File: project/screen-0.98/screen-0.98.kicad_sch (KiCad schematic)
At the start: 34 parts, among them J1 TFT_0.96_13, J2 Conn_01x06_Female, J3 USB_C_6pin, J4 Conn_01x02_Female, SW1 SW_DPDT_x2, SW2 SW_Push, SW3 SW_Push, U1 SPX3819M5-L-3-3, U2 ESP-12E, U3 TP4056_[C16581]

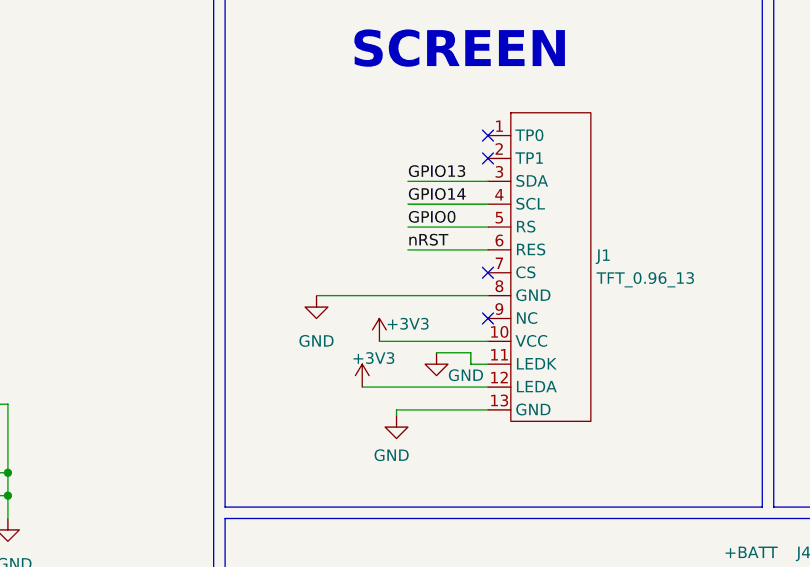
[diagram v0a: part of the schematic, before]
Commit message: fix: screen rst and cs
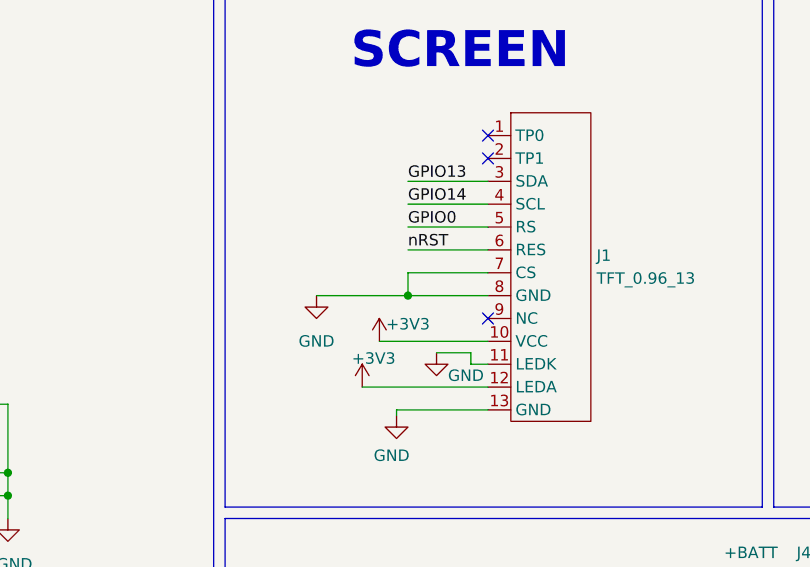
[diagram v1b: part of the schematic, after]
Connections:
- net GND: now also J1.7 (CS)
- no-connect marks 13 -> 12
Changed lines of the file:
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@@
   (junction (at 152.4 139.7) (diameter 0) (color 0 0 0 0)
+  )
+  (junction (at 196.85 117.475) (diameter 0) (color 0 0 0 0)
   )
   (junction (at 31.75 149.86) (diameter 0) (color 0 0 0 0)
@@
   (no_connect (at 85.09 49.53))
   (no_connect (at 50.8 129.54))
-  (no_connect (at 205.74 114.935))
   (no_connect (at 238.76 48.26))
   (no_connect (at 85.09 52.07))
@@
     (stroke (width 0) (type default) (color 0 0 0 0))
   )
+  (wire (pts (xy 205.74 114.935) (xy 196.85 114.935))
+    (stroke (width 0) (type default) (color 0 0 0 0))
+  )
   (polyline (pts (xy 176.53 80.01) (xy 236.22 80.01))
     (stroke (width 0) (type default) (color 0 0 0 0))
@@
     (stroke (width 0) (type default) (color 0 0 0 0))
   )
+  (wire (pts (xy 196.85 117.475) (xy 205.74 117.475))
+    (stroke (width 0) (type default) (color 0 0 0 0))
+  )
   (polyline (pts (xy 12.7 12.7) (xy 12.7 78.74))
     (stroke (width 0) (type default) (color 0 0 0 0))
@@
     (stroke (width 0) (type default) (color 0 0 0 0))
   )
+  (wire (pts (xy 196.85 114.935) (xy 196.85 117.475))
+    (stroke (width 0) (type default) (color 0 0 0 0))
+  )
   (wire (pts (xy 64.77 62.23) (xy 64.77 64.77))
     (stroke (width 0) (type default) (color 0 0 0 0))
@@
     (stroke (width 0) (type default) (color 0 0 0 0))
   )
-  (wire (pts (xy 186.69 117.475) (xy 205.74 117.475))
-    (stroke (width 0) (type default) (color 0 0 0 0))
-  )
+  (wire (pts (xy 186.69 117.475) (xy 196.85 117.475))
+    (stroke (width 0) (type default) (color 0 0 0 0))
+  )

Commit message: update 0.98
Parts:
- added Q1: S8050, Package_TO_SOT_SMD:SOT-23, symbol Device:Q_NPN_BEC
- added R15: 1K, Resistor_SMD:R_0402_1005Metric, symbol Device:R
- added R16: 12K, Resistor_SMD:R_0402_1005Metric, symbol Device:R
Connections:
- net +3V3: now also R16.1
- net GND: now also Q1.2 (E); no longer J1.11 (LEDK)
- net GPIO2: now also J1.6 (RES)
- net GPIO5: now also R15.1
- net nRST: no longer J1.6 (RES)
- new net: Q1.1 (B), R15.2, R16.2
- new net: J1.11 (LEDK), Q1.3 (C)
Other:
- moved on the sheet: J1

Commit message: feat: screen v1.3 done
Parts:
- removed J2: Conn_01x06_Female, Connector_PinHeader_1.27mm:PinHeader_1x06_P1.27mm_Vertical, symbol Connector:Conn_01x06_Female
- added J?: TTL-connect-pin4, symbol My-lib:TTL-connect-pin4
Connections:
- net GND: now also J?.1 (GND)
- net GPIO0: now also J?.2 (GPIO0)
- net RXD: now also J?.3 (RXD)
- net TXD: now also J?.4 (TXD)
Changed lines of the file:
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@@
-    (stroke (width 0) (type default) (color 0 0 0 0))
-  )
-  (wire (pts (xy 256.54 124.46) (xy 265.43 124.46))
     (stroke (width 0) (type default) (color 0 0 0 0))
   )
@@
     (stroke (width 0) (type default) (color 0 0 0 0))
   )
-  (wire (pts (xy 256.54 119.38) (xy 265.43 119.38))
-    (stroke (width 0) (type default) (color 0 0 0 0))
-  )
   (wire (pts (xy 31.75 149.86) (xy 31.75 151.13))
     (stroke (width 0) (type default) (color 0 0 0 0))
@@
     (stroke (width 0) (type default) (color 0 0 0 0))
   )
+  (wire (pts (xy 251.46 117.475) (xy 258.445 117.475))
+    (stroke (width 0) (type default) (color 0 0 0 0))
+  )
   (wire (pts (xy 175.26 57.15) (xy 182.88 57.15))
     (stroke (width 0) (type default) (color 0 0 0 0))
@@
     (stroke (width 0) (type default) (color 0 0 0 0))
   )
+  (wire (pts (xy 249.555 109.855) (xy 258.445 109.855))
+    (stroke (width 0) (type default) (color 0 0 0 0))
+  )
   (wire (pts (xy 200.914 119.38) (xy 211.074 119.38))
     (stroke (width 0) (type default) (color 0 0 0 0))
@@
     (stroke (width 0) (type default) (color 0 0 0 0))
   )
-  (wire (pts (xy 252.73 116.84) (xy 265.43 116.84))
+  (wire (pts (xy 249.555 114.935) (xy 258.445 114.935))
     (stroke (width 0) (type default) (color 0 0 0 0))
   )
@@
     (stroke (width 0) (type default) (color 0 0 0 0))
   )
-  (wire (pts (xy 256.54 127) (xy 265.43 127))
-    (stroke (width 0) (type default) (color 0 0 0 0))
-  )
   (wire (pts (xy 115.57 41.91) (xy 124.46 41.91))
     (stroke (width 0) (type default) (color 0 0 0 0))
@@
     (stroke (width 0) (type default) (color 0 0 0 0))
   )
-  (wire (pts (xy 256.54 121.92) (xy 265.43 121.92))
-    (stroke (width 0) (type default) (color 0 0 0 0))
-  )
   (wire (pts (xy 100.33 147.32) (xy 100.33 142.24))
     (stroke (width 0) (type default) (color 0 0 0 0))
@@
     (stroke (width 0) (type default) (color 0 0 0 0))
   )
-  (wire (pts (xy 256.54 114.3) (xy 265.43 114.3))
-    (stroke (width 0) (type default) (color 0 0 0 0))
-  )
   (wire (pts (xy 96.52 137.16) (xy 100.33 137.16))
     (stroke (width 0) (type default) (color 0 0 0 0))
@@
   )
   (polyline (pts (xy 237.49 80.01) (xy 284.48 80.01))
+    (stroke (width 0) (type default) (color 0 0 0 0))
+  )
+  (wire (pts (xy 249.555 112.395) (xy 258.445 112.395))
     (stroke (width 0) (type default) (color 0 0 0 0))
   )
@@
     (effects (font (size 1.27 1.27)) (justify right bottom))
   )
-  (label "GPIO0" (at 256.54 121.92 0)
-    (effects (font (size 1.27 1.27)) (justify left bottom))
-  )
   (label "ADC" (at 76.2 41.91 0)
     (effects (font (size 1.27 1.27)) (justify left bottom))
@@
     (effects (font (size 1.27 1.27)) (justify right bottom))
   )
+  (label "RXD" (at 249.555 112.395 0)
+    (effects (font (size 1.27 1.27)) (justify left bottom))
+  )
   (label "GPIO12" (at 124.46 46.99 180)
     (effects (font (size 1.27 1.27)) (justify right bottom))
@@
     (effects (font (size 1.27 1.27)) (justify right bottom))
   )
-  (label "TXD" (at 256.54 124.46 0)
-    (effects (font (size 1.27 1.27)) (justify left bottom))
-  )
   (label "GPIO15" (at 124.46 54.61 180)
     (effects (font (size 1.27 1.27)) (justify right bottom))
@@
     (effects (font (size 1.27 1.27)) (justify right bottom))
   )
+  (label "TXD" (at 249.555 109.855 0)
+    (effects (font (size 1.27 1.27)) (justify left bottom))
+  )
+  (label "GPIO0" (at 249.555 114.935 0)
+    (effects (font (size 1.27 1.27)) (justify left bottom))
+  )
   (label "GPIO14" (at 211.074 109.22 0)
     (effects (font (size 1.27 1.27)) (justify left bottom))
@@
     (effects (font (size 1.27 1.27)) (justify right bottom))
   )
-  (label "RXD" (at 256.54 127 0)
-    (effects (font (size 1.27 1.27)) (justify left bottom))
-  )
   (label "GPIO2" (at 124.46 36.83 180)
     (effects (font (size 1.27 1.27)) (justify right bottom))
@@
   (label "GPIO15" (at 58.42 59.69 180)
     (effects (font (size 1.27 1.27)) (justify right bottom))
-  )
-  (label "nRST" (at 256.54 119.38 0)
-    (effects (font (size 1.27 1.27)) (justify left bottom))
   )
   (label "GPIO4" (at 124.46 41.91 180)
@@
     (pin "1")
     (pin "2")
-  )
-  (symbol (lib_id "Connector:Conn_01x06_Female") (at 270.51 119.38 0) (unit 1)
-    (in_bom yes) (on_board yes)
-    (property "Reference" "J2" (id 0) (at 264.16 109.22 0)
-      (effects (font (size 1.27 1.27)) (justify left))
-    )
-    (property "Value" "Conn_01x06_Female" (id 1) (at 255.27 132.08 0)
-      (effects (font (size 1.27 1.27)) (justify left))
-    )
-    (property "Footprint" "Connector_PinHeader_1.27mm:PinHeader_1x06_P1.27mm_Vertical" (id 2) (at 270.51 119.38 0)
-      (effects (font (size 1.27 1.27)) hide)
-    )
-    (property "Datasheet" "~" (id 3) (at 270.51 119.38 0)
-      (effects (font (size 1.27 1.27)) hide)
-    )
-    (pin "1")
-    (pin "2")
-    (pin "3")
-    (pin "4")
-    (pin "5")
-    (pin "6")
   )
   (symbol (lib_id "power:GND") (at 100.33 171.45 0) (unit 1)
@@
     (pin "2")
   )
-  (symbol (lib_id "power:+3V3") (at 256.54 114.3 0) (unit 1)
-    (in_bom yes) (on_board yes)
-    (property "Reference" "#PWR016" (id 0) (at 256.54 118.11 0)
-      (effects (font (size 1.27 1.27)) hide)
-    )
-    (property "Value" "+3V3" (id 1) (at 256.54 109.22 0))
-    (property "Footprint" "" (id 2) (at 256.54 114.3 0)
-      (effects (font (size 1.27 1.27)) hide)
-    )
-    (property "Datasheet" "" (id 3) (at 256.54 114.3 0)
-      (effects (font (size 1.27 1.27)) hide)
-    )
-    (pin "1")
-  )
   (symbol (lib_id "Switch:SW_Push") (at 182.88 62.23 270) (unit 1)
     (in_bom yes) (on_board yes) (fields_autoplaced)
@@
     (pin "2")
   )
+  (symbol (lib_id "My-lib:TTL-connect-pin4") (at 263.525 113.665 0) (unit 1)
+    (in_bom yes) (on_board yes)
+    (property "Reference" "J?" (id 0) (at 262.255 106.68 0)
+      (effects (font (size 1.27 1.27)) (justify left))
+    )
+    (property "Value" "TTL-connect-pin4" (id 1) (at 255.905 121.285 0)
+      (effects (font (size 1.27 1.27)) (justify left))
+    )
+    (property "Footprint" "" (id 2) (at 262.255 111.125 0)
+      (effects (font (size 1.27 1.27)) hide)
+    )
+    (property "Datasheet" "" (id 3) (at 262.255 111.125 0)
+      (effects (font (size 1.27 1.27)) hide)
+    )
+    (pin "1")
+    (pin "2")
+    (pin "3")
+    (pin "4")
+  )
   (symbol (lib_id "My-lib:USB_C_6pin") (at 35.56 127 0) (unit 1)
     (in_bom yes) (on_board yes) (fields_autoplaced)
@@
     (pin "2")
   )
+  (symbol (lib_id "power:GND") (at 251.46 117.475 0) (mirror y) (unit 1)
+    (in_bom yes) (on_board yes)
+    (property "Reference" "#PWR?" (id 0) (at 251.46 123.825 0)
+      (effects (font (size 1.27 1.27)) hide)
+    )
+    (property "Value" "GND" (id 1) (at 251.46 121.285 0))
+    (property "Footprint" "" (id 2) (at 251.46 117.475 0)
+      (effects (font (size 1.27 1.27)) hide)
+    )
+    (property "Datasheet" "" (id 3) (at 251.46 117.475 0)
+      (effects (font (size 1.27 1.27)) hide)
+    )
+    (pin "1")
+  )
   (symbol (lib_id "Device:R") (at 184.404 109.22 0) (mirror y) (unit 1)
     (in_bom yes) (on_board yes)
@@
     (pin "2")
   )
-  (symbol (lib_id "power:GND") (at 252.73 116.84 0) (mirror y) (unit 1)
-    (in_bom yes) (on_board yes)
-    (property "Reference" "#PWR017" (id 0) (at 252.73 123.19 0)
-      (effects (font (size 1.27 1.27)) hide)
-    )
-    (property "Value" "GND" (id 1) (at 252.73 120.65 0))
-    (property "Footprint" "" (id 2) (at 252.73 116.84 0)
-      (effects (font (size 1.27 1.27)) hide)
-    )
-    (property "Datasheet" "" (id 3) (at 252.73 116.84 0)
-      (effects (font (size 1.27 1.27)) hide)
-    )
-    (pin "1")
-  )
   (symbol (lib_id "power:GND") (at 55.88 124.46 0) (mirror y) (unit 1)
     (in_bom yes) (on_board yes)
@@
       (reference "#PWR015") (unit 1) (value "GND") (footprint "")
     )
-    (path "/a41c656b-c1d5-4600-8933-88a1e064dd0d"
-      (reference "#PWR016") (unit 1) (value "+3V3") (footprint "")
-    )
-    (path "/fb7892a0-29e9-4d08-86e9-ed9ad1c00745"
-      (reference "#PWR017") (unit 1) (value "GND") (footprint "")
-    )
     (path "/1d9e88c6-6ff6-49b8-b9eb-eed04e15bea8"
       (reference "#PWR018") (unit 1) (value "GND") (footprint "")
@@
       (reference "#PWR031") (unit 1) (value "+3V3") (footprint "")
     )
+    (path "/ef4cc696-76b5-4a76-9c87-07c3266f5c5a"
+      (reference "#PWR?") (unit 1) (value "GND") (footprint "")
+    )
     (path "/11a364a0-8d31-431e-8b25-ceb35237b885"
       (reference "C1") (unit 1) (value "100uf") (footprint "lc_lib:CASE-B_3528")
@@
       (reference "J1") (unit 1) (value "TFT_0.96_13") (footprint "My-lib-footprints:TFT_0.96_13_front")
     )
-    (path "/11abb483-9dcd-4c33-a370-d7ce03952760"
-      (reference "J2") (unit 1) (value "Conn_01x06_Female") (footprint "Connector_PinHeader_1.27mm:PinHeader_1x06_P1.27mm_Vertical")
-    )
     (path "/dd90ac7e-3f2c-416b-9b68-cd5b2f6ea0ad"
       (reference "J3") (unit 1) (value "USB_C_6pin") (footprint "My-lib-footprints:USB_C_6pin")
@@
       (reference "J4") (unit 1) (value "Conn_01x02_Female") (footprint "Connector_PinHeader_2.54mm:PinHeader_1x02_P2.54mm_Vertical")
     )
+    (path "/dbd9f3b3-07ea-4091-963e-ae481a860bdc"
+      (reference "J?") (unit 1) (value "TTL-connect-pin4") (footprint "")
+    )
     (path "/377817d1-84c7-444b-b966-48eb3b02923d"
